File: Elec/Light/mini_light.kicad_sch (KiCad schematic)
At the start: 18 parts, among them J1 Conn_01x03, J2 Conn_01x03, U1 AL8860WT-7

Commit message: Update lib and pcb
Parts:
- removed J1, J2: Conn_01x03, Connector_JST:JST_PH_S3B-PH-SM4-TB_1x03-1MP_P2.00mm_Horizontal, symbol Connector_Generic:Conn_01x03
- added J1, J2: Conn_01x03_MountingPin, Connector_JST:JST_PH_S3B-PH-SM4-TB_1x03-1MP_P2.00mm_Horizontal, symbol Connector_Generic_MountingPin:Conn_01x03_MountingPin
- D2, D3, D4, D5, D6, D7: footprint mini_light:LED_Cree-JE -> AM163:LED_Cree-JE
- L1: footprint mini_light:L_Bourns-SRN5040 -> AM163:L_Bourns-SRN5040
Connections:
- net +12V: now also J1.3 (Pin_3), J2.1 (Pin_1)
- net Ctrl: now also J1.1 (Pin_1), J2.3 (Pin_3)
- net GND: now also J1.2 (Pin_2), J1.MP (MountPin), J2.2 (Pin_2), J2.MP (MountPin)

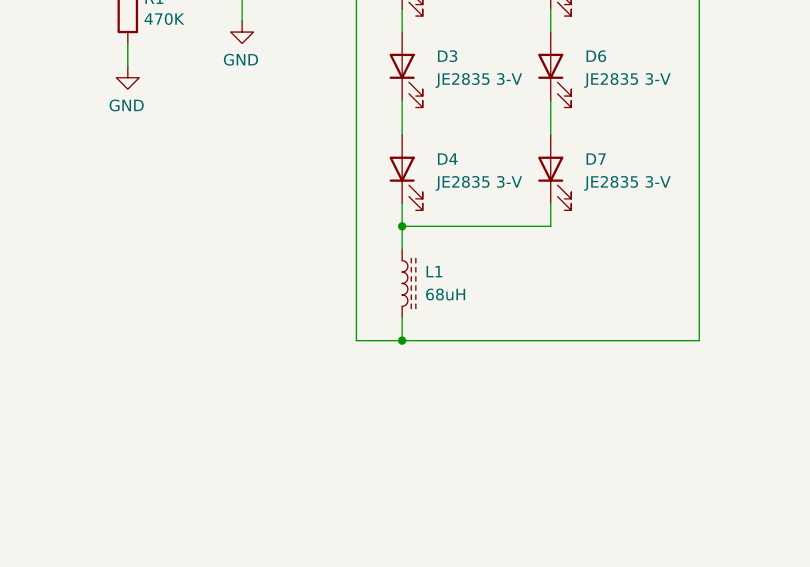
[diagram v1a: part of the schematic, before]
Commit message: Change JST connector polarity + regenerate gerber file
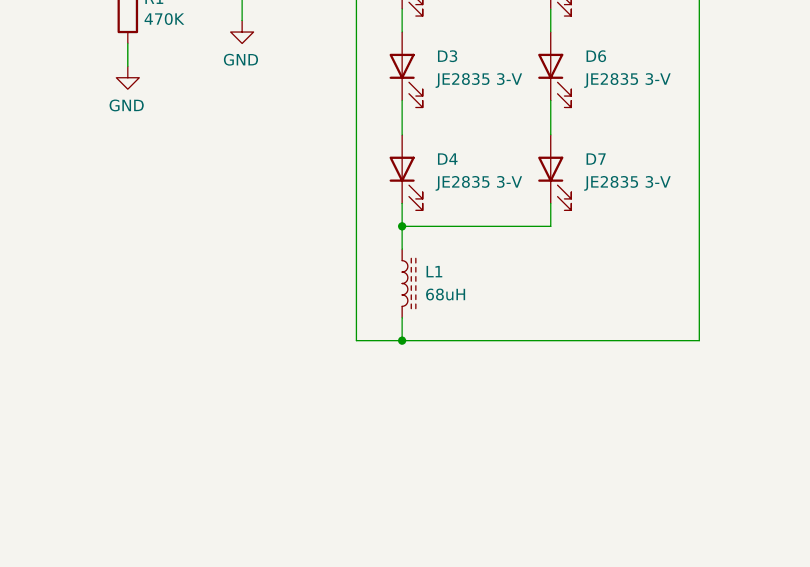
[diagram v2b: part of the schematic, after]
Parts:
- U1: symbol antoine163:AL8860WT-7 -> AM163:AL8860WT-7
